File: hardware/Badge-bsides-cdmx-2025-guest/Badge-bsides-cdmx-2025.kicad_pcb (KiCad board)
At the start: 2 copper layers, 50 x 110 mm, 30 parts, among them J1 SWDIO, J3 ADDON, J4 Conn_01x04_Pin, J5 I2C, J6 Conn_01x04_Pin, P6 USB_C_Plug_USB2.0, Q3 DMG3415U-7, SW11 ON, SW2 RESET, U1 PY32F030F28U6TR, U6 AP2112K-3.3

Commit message: feat(Hw):started_routing
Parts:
- added C67: 10uF, Capacitor_SMD:C_0603_1608Metric, B.Cu at (153.4, 61.0)
- added C68: 10uF, Capacitor_SMD:C_0603_1608Metric, B.Cu at (143.7, 61.0)
- added C69: 10uF, Capacitor_SMD:C_0603_1608Metric, B.Cu at (134.4, 61.5)
- added C70: 10uF, Capacitor_SMD:C_0603_1608Metric, B.Cu at (124.5, 63.0)
- added R5: 10k, Resistor_SMD:R_0603_1608Metric, B.Cu at (153.4, 62.5)
- added R6: 10k, Resistor_SMD:R_0603_1608Metric, B.Cu at (143.7, 62.5)
- added R7: 10k, Resistor_SMD:R_0603_1608Metric, B.Cu at (134.4, 63.0)
- added R8: 10k, Resistor_SMD:R_0603_1608Metric, B.Cu at (124.5, 61.5)
- added SW10: SW_Push, Footprints:TS1088R02026, F.Cu at (124.7, 62.0)
- added SW7: SW_Push, Footprints:TS1088R02026, F.Cu at (134.4, 62.0)
- added SW8: SW_Push, Footprints:TS1088R02026, F.Cu at (153.7, 62.0)
- added SW9: SW_Push, Footprints:TS1088R02026, F.Cu at (144.2, 62.0)
- BT3, BT4, J4: moved to B.Cu
- J3, J5: moved to F.Cu
- moved J1 57.5 mm to (116.2, 68.1)
- moved BT3 44.7 mm to (160.1, 111.2), turned to 180 degrees
- moved J3 41.3 mm to (119.3, 40.3), turned to 90 degrees
- moved R41 38.5 mm to (157.3, 66.5)
- moved D10 38.2 mm to (129.9, 93.3)
- moved BT4 37.9 mm to (160.5, 137.1), turned to 180 degrees
- moved R11 37.7 mm to (130.4, 96.3), turned to 180 degrees
- moved C33 35.8 mm to (151.0, 67.9)
- moved C10 34.9 mm to (126.3, 75.0)
- moved C26 34.9 mm to (130.5, 73.5)
- moved U6 34.9 mm to (126.8, 72.5)
- moved F3 34.4 mm to (151.0, 70.9)
- moved C27 33.0 mm to (151.0, 69.4)
- moved P6 32.8 mm to (156.3, 73.3)
- moved SW11 31.3 mm to (117.0, 76.0)
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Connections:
- BT3 pad 2: +3.3V -> +BATT
- J3 pad 5: /GPIO1 -> /GPIO2
- J3 pad 6: /GPIO2 -> /GPIO1
- U1 pad 1: unconnected-(U1-PA5-Pad1) -> /BTTN2
- U1 pad 10: unconnected-(U1-PB6-Pad10) -> /LED1
- U1 pad 16: /GPIO2 -> /BTTN4
- U1 pad 17: /GPIO1 -> /BTTN3
- U1 pad 2: /LED1 -> /BTTN1
- U1 pad 20: unconnected-(U1-PA4-Pad20) -> /LED2
- U1 pad 3: /LED2 -> /GPIO1
- U1 pad 5: unconnected-(U1-PA12-Pad5) -> /GPIO2
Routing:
- net /TX: track 0.00 -> 2.54 mm
- net /RX: track 0.00 -> 2.54 mm
- net /BTTN4: track 0.00 -> 1.52 mm
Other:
- board size 50 x 110 mm -> 50.1 x 110 mm

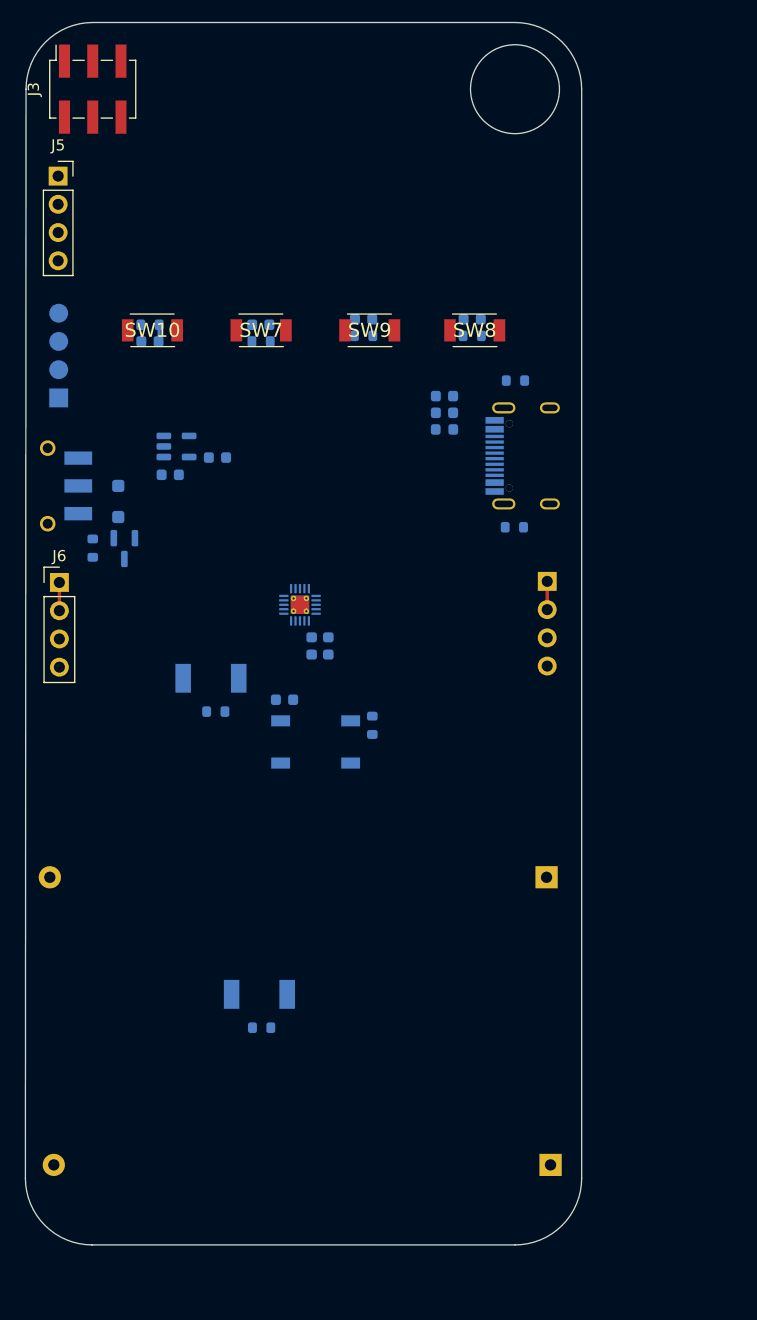
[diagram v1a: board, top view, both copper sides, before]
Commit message: feat(Hw):Route_Sponsor
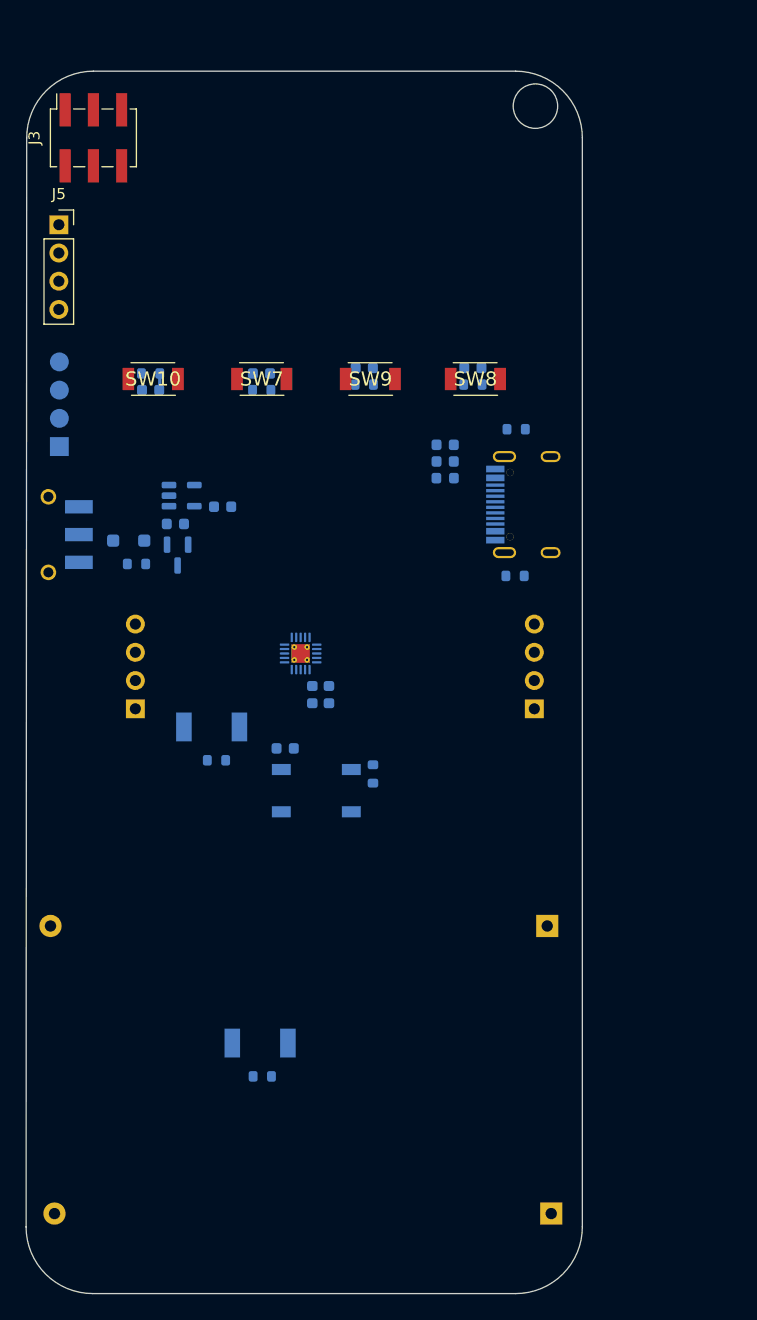
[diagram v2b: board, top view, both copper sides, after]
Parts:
- J4: footprint Connector_PinHeader_2.54mm:PinHeader_1x04_P2.54mm_Vertical -> Connector_PinHeader_2.54mm:PinHeader_1x04_P2.54mm_Horizontal
- J6: footprint Connector_PinHeader_2.54mm:PinHeader_1x04_P2.54mm_Vertical -> Connector_PinSocket_2.54mm:PinSocket_1x04_P2.54mm_Horizontal; moved to B.Cu
- moved J6 13.3 mm to (123.1, 96.1)
- moved J4 11.5 mm to (159.0, 96.1), turned to 0 degrees
- moved Q3 4.82 mm to (126.9, 82.2)
- moved C10 4.45 mm to (126.7, 79.4)
- moved C26 4.45 mm to (131.0, 77.9)
- moved U6 4.45 mm to (127.3, 76.9)
- moved C6 4.38 mm to (136.6, 99.6)
- moved P6 4.38 mm to (156.4, 77.7)
- moved R41 4.38 mm to (157.4, 70.9)
- moved R9 4.38 mm to (134.6, 129.1)
- moved J3 4.38 mm to (119.4, 44.7)
- moved J5 4.38 mm to (116.2, 52.5)
- moved BT3 4.38 mm to (160.2, 115.6)
- moved BT4 4.38 mm to (160.6, 141.5)
- moved C27 4.38 mm to (151.0, 73.8)
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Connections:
- J4 pad 1: /RX -> GND
- J4 pad 2: /RX -> GND
- J4 pad 3: GND -> /RX
- J4 pad 4: GND -> /RX
- J6 pad 1: /TX -> GND
- J6 pad 2: /TX -> GND
- J6 pad 3: GND -> /TX
- J6 pad 4: GND -> /TX
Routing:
- net /TX: track 2.54 -> 0.00 mm
- net /RX: track 2.54 -> 0.00 mm
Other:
- outline, holes or cut-outs redrawn

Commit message: Auto stash before merge of "main" and "origin/main"
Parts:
- removed C10, C27: 10uF, Capacitor_SMD:C_0603_1608Metric
- removed D10, D9: R_LED, Footprints:LYT77K-K2M1
- removed D4: MBR120, Diode_SMD:D_SOD-123F
- removed F3: 750mA, Fuse:Fuse_0603_1608Metric
- removed P6: USB_C_Plug_USB2.0, Footprints:C393939
- removed Q3: DMG3415U-7, Package_TO_SOT_SMD:SOT-23
- removed R10: 100K, Resistor_SMD:R_0603_1608Metric
- removed R11, R9: 220, Resistor_SMD:R_0603_1608Metric
- removed R41, R45: 5k1, Resistor_SMD:R_0603_1608Metric
- removed U6: AP2112K-3.3, Package_TO_SOT_SMD:SOT-23-5
- added C31: 100nF, Capacitor_SMD:C_0603_1608Metric, B.Cu at (127.8, 95.8)
- added C32: 100nF, Capacitor_SMD:C_0603_1608Metric, B.Cu at (137.1, 129.5)
- added D21: SK6812MINI-E, Footprints:LED_SK6812-E, B.Cu at (130.1, 98.3)
- added D22: SK6812MINI-E, Footprints:LED_SK6812-E, B.Cu at (134.6, 127.0)
- added R12: 1K, Resistor_SMD:R_0603_1608Metric, B.Cu at (132.4, 95.8)
- added kibuzzard-684312AE: G***, kibuzzard-684312AE, B.Cu at (115.3, 74.8)
- added kibuzzard-684312C0: G***, kibuzzard-684312C0, B.Cu at (115.4, 85.9)
- added kibuzzard-684312D7: G***, kibuzzard-684312D7, B.Cu at (151.1, 60.3)
- added kibuzzard-684312EA: G***, kibuzzard-684312EA, F.Cu at (114.4, 43.7)
- added kibuzzard-684312F6: G***, kibuzzard-684312F6, F.Cu at (114.3, 46.8)
- added kibuzzard-68431305: G***, kibuzzard-68431305, B.Cu at (116.9, 57.5)
- added kibuzzard-6843130E: G***, kibuzzard-6843130E, B.Cu at (117.0, 60.3)
- moved C6 48.4 mm to (148.1, 52.6)
- moved SW2 48.4 mm to (150.8, 56.4)
- moved R4 47.1 mm to (145.8, 54.9)
- moved BT3 44.0 mm to (116.2, 116.0), turned to 0 degrees
- moved C33 27.6 mm to (123.8, 77.0), turned to 90 degrees
- moved C34 15.6 mm to (138.7, 79.2), turned to 90 degrees
- moved C28 14.4 mm to (136.4, 81.0), turned to 180 degrees
- moved C26 8.73 mm to (122.3, 77.0), turned to 90 degrees
- moved U1 8.48 mm to (140.1, 82.8), turned to 0 degrees
- moved J5 4.75 mm to (121.0, 52.5)
- moved BT4 3.48 mm to (160.6, 138.0)
- moved R8 1.52 mm to (124.5, 67.4)
- moved C70 1.48 mm to (124.5, 65.9)
- moved J6 0.36 mm to (123.5, 96.0)
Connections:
- BT3 pad 1: Net-(BT3--) -> +BATT
- BT3 pad 2: +BATT -> Net-(BT3--)
- BT4 pad 1: GND -> Net-(BT3--)
- BT4 pad 2: Net-(BT3--) -> GND
- C26 pad 1: +3V3 -> +3.3V
- C33 pad 1: VBUS -> +3.3V
- J3 pad 1: +3V3 -> +3.3V
- J4 pad 3: /RX -> /TX
- J4 pad 4: /RX -> /TX
- J6 pad 3: /TX -> /RX
- J6 pad 4: /TX -> /RX
- R4 pad 2: +3V3 -> +3.3V
- R5 pad 2: +3V3 -> +3.3V
- R6 pad 2: +3V3 -> +3.3V
- R7 pad 2: +3V3 -> +3.3V
- R8 pad 2: +3V3 -> +3.3V
- SW11 pad 2: Net-(D4-K) -> +BATT
- SW11 pad 3: Net-(SW11-A) -> +3.3V
- U1 pad 10: /LED1 -> unconnected-(U1-PB6-Pad10)
- U1 pad 11: unconnected-(U1-PB7-Pad11) -> /GPIO1
- U1 pad 12: unconnected-(U1-PF4/BOOT0-Pad12) -> /GPIO2
- U1 pad 20: /LED2 -> unconnected-(U1-PA4-Pad20)
- U1 pad 3: /GPIO1 -> /NEO
- U1 pad 5: /GPIO2 -> unconnected-(U1-PA12-Pad5)
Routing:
- net +3.3V: track 0.07 -> 206.7 mm
- net /GPIO2: track 0.00 -> 71.9 mm, vias 0 -> 3
- net /SDA: track 0.00 -> 71.9 mm, vias 0 -> 2
- net /SCL: track 0.03 -> 69.0 mm, vias 0 -> 1
- net /GPIO1: track 0.00 -> 66.4 mm, vias 0 -> 3
- net /NTST: track 0.00 -> 47.0 mm, vias 0 -> 2
- net /BTTN1: track 0.00 -> 42.5 mm, vias 0 -> 2
- net +BATT: track 0.00 -> 40.0 mm
- net /BTTN4: track 1.52 -> 41.2 mm, vias 0 -> 2
- net /SWCLK: track 0.00 -> 37.1 mm, vias 0 -> 2
- net /SWDIO: track 0.00 -> 34.0 mm, vias 0 -> 2
- net /BTTN2: track 0.00 -> 33.2 mm, vias 0 -> 2
- net /BTTN3: track 0.00 -> 32.9 mm, vias 0 -> 2
- net Net-(D21-DOUT): track 0.00 -> 31.7 mm
- net /TX: track 0.00 -> 25.2 mm, vias 0 -> 1
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- added copper zone on B.Cu, net +3.3V
- added copper zone on B.Cu, net GND
- added copper zone on F.Cu, net GND
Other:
- board size 50.1 x 110 mm -> 49.9 x 109.8 mm

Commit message: fix(Hw):Labels_Updated
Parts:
- R12: value 1K -> 470R
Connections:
- U1 pad 21: (no net) -> GND
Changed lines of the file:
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@@
 			(layers "*.Cu")
 			(remove_unused_layers no)
+			(net 1 "GND")
+			(pinfunction "VSS")
+			(pintype "bidirectional")
 		)
 		(pad "21" thru_hole circle
@@
 			(layers "*.Cu")
 			(remove_unused_layers no)
+			(net 1 "GND")
+			(pinfunction "VSS")
+			(pintype "bidirectional")
 		)
 		(pad "21" smd rect
@@
 			(property pad_prop_heatsink)
 			(layers "F.Cu")
+			(net 1 "GND")
+			(pinfunction "VSS")
+			(pintype "bidirectional")
 			(zone_connect 2)
 		)
@@
 			(property pad_prop_heatsink)
 			(layers "B.Cu" "B.Mask")
+			(net 1 "GND")
+			(pinfunction "VSS")
+			(pintype "bidirectional")
 			(zone_connect 2)
 		)
@@
 			(layers "*.Cu")
 			(remove_unused_layers no)
+			(net 1 "GND")
+			(pinfunction "VSS")
+			(pintype "bidirectional")
 		)
 		(pad "21" thru_hole circle
@@
 			(layers "*.Cu")
 			(remove_unused_layers no)
+			(net 1 "GND")
+			(pinfunction "VSS")
+			(pintype "bidirectional")
 		)
 		(embedded_fonts no)
@@
 			)
 		)
-		(property "Value" "1K"
+		(property "Value" "470R"
 			(at 0 -1.43 0)
 			(layer "B.Fab")
@@
 			)
 		)
-		(property "LCSC#" "C22548"
+		(property "LCSC#" "C114669"
 			(at 0 0 180)
 			(unlocked yes)
